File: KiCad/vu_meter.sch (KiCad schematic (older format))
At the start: 74 parts

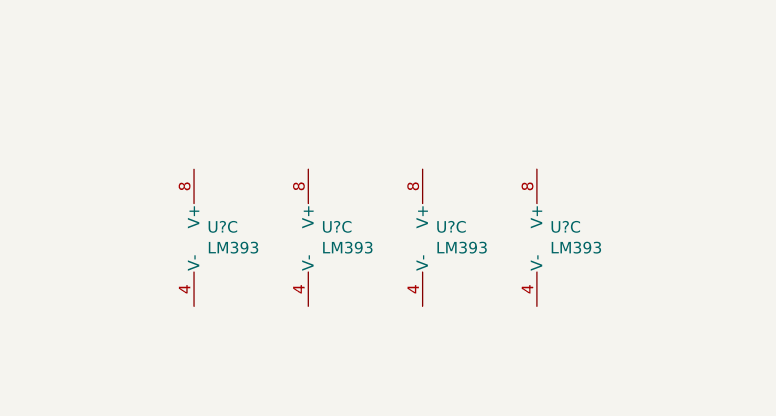
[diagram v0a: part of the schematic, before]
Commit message: freeze at 3 leds
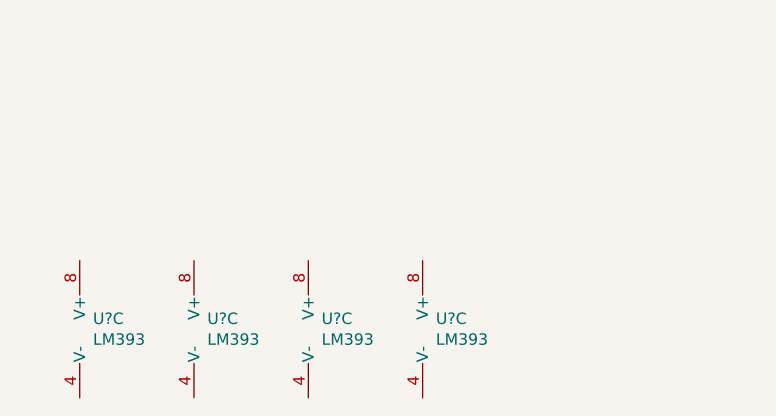
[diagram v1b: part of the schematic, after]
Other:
- moved on the sheet: U?C
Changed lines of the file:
@@
 L Amp-Module-rescue:LM393-Comparator-Amp-Module-rescue U?
 U 3 1 60A35849
-P 1300 6950
+P 800 7350
 AR Path="/604C8E92/60793AB8/60A35849" Ref="U?"  Part="3"
 AR Path="/604C8E92/60A35849" Ref="U?"  Part="3"
 AR Path="/60A35849" Ref="U?"  Part="3"
-F 0 "U?" H 1258 6996 50  0000 L CNN
-F 1 "LM393" H 1258 6905 50  0000 L CNN
-F 2 "" H 1300 6950 50  0001 C CNN
-F 3 "" H 1300 6950 50  0001 C CNN
-	3    1300 6950
+F 0 "U?" H 758 7396 50  0000 L CNN
+F 1 "LM393" H 758 7305 50  0000 L CNN
+F 2 "" H 800 7350 50  0001 C CNN
+F 3 "" H 800 7350 50  0001 C CNN
+	3    800  7350
 	1    0    0    -1
 $EndComp
@@
 L Amp-Module-rescue:LM393-Comparator-Amp-Module-rescue U?
 U 3 1 60A3585D
-P 1800 6950
+P 1300 7350
 AR Path="/604C8E92/60793AB8/60A3585D" Ref="U?"  Part="3"
 AR Path="/604C8E92/60A3585D" Ref="U?"  Part="3"
 AR Path="/60A3585D" Ref="U?"  Part="3"
-F 0 "U?" H 1758 6996 50  0000 L CNN
-F 1 "LM393" H 1758 6905 50  0000 L CNN
-F 2 "" H 1800 6950 50  0001 C CNN
-F 3 "" H 1800 6950 50  0001 C CNN
-	3    1800 6950
+F 0 "U?" H 1258 7396 50  0000 L CNN
+F 1 "LM393" H 1258 7305 50  0000 L CNN
+F 2 "" H 1300 7350 50  0001 C CNN
+F 3 "" H 1300 7350 50  0001 C CNN
+	3    1300 7350
 	1    0    0    -1
 $EndComp
@@
 L Amp-Module-rescue:LM393-Comparator-Amp-Module-rescue U?
 U 3 1 60A35997
-P 2300 6950
+P 1800 7350
 AR Path="/604C8E92/60793AB8/60A35997" Ref="U?"  Part="3"
 AR Path="/604C8E92/60A35997" Ref="U?"  Part="3"
 AR Path="/60A35997" Ref="U?"  Part="3"
-F 0 "U?" H 2258 6996 50  0000 L CNN
-F 1 "LM393" H 2258 6905 50  0000 L CNN
-F 2 "" H 2300 6950 50  0001 C CNN
-F 3 "" H 2300 6950 50  0001 C CNN
-	3    2300 6950
+F 0 "U?" H 1758 7396 50  0000 L CNN
+F 1 "LM393" H 1758 7305 50  0000 L CNN
+F 2 "" H 1800 7350 50  0001 C CNN
+F 3 "" H 1800 7350 50  0001 C CNN
+	3    1800 7350
 	1    0    0    -1
 $EndComp
@@
 L Amp-Module-rescue:LM393-Comparator-Amp-Module-rescue U?
 U 3 1 60A3599D
-P 2800 6950
+P 2300 7350
 AR Path="/604C8E92/60793AB8/60A3599D" Ref="U?"  Part="3"
 AR Path="/604C8E92/60A3599D" Ref="U?"  Part="3"
 AR Path="/60A3599D" Ref="U?"  Part="3"
-F 0 "U?" H 2758 6996 50  0000 L CNN
-F 1 "LM393" H 2758 6905 50  0000 L CNN
-F 2 "" H 2800 6950 50  0001 C CNN
-F 3 "" H 2800 6950 50  0001 C CNN
-	3    2800 6950
-	1    0    0    -1
-$EndComp
+F 0 "U?" H 2258 7396 50  0000 L CNN
+F 1 "LM393" H 2258 7305 50  0000 L CNN
+F 2 "" H 2300 7350 50  0001 C CNN
+F 3 "" H 2300 7350 50  0001 C CNN
+	3    2300 7350
+	1    0    0    -1
+$EndComp

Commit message: schematic completed
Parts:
- removed D? (x3): LED_Small, symbol Device:LED_Small
- removed D?: 3V, symbol Device:D_Zener_Small
- removed D?: 2V, symbol Device:D_Zener_Small
- removed Q? (x4): NPN, symbol Device:Q_NPN_BCE
- removed Q?: PNP, symbol Device:Q_PNP_BCE
- removed R?: 75, symbol Device:R_Small
- removed R?: 20k, symbol Device:R_Small
- removed R?: 15k, symbol Device:R_Small
- removed R?: 23k, symbol Device:R_Small
- removed R? (x6): 10k, symbol Device:R_Small
- removed R?: 100k, symbol Device:R_Small
- removed R?: 150, symbol Device:R_Small
- removed R? (x3): 22k, symbol Device:R_Small
- removed R?: 12k, symbol Device:R_Small
- removed R?: 33k, symbol Device:R_Small
- removed R?: 27k, symbol Device:R_Small
- removed R?: 36k, symbol Device:R_Small
- removed R? (x2): 120k, symbol Device:R_Small
- removed U? (x12): LM393, symbol Amp-Module-rescue:LM393-Comparator-Amp-Module-rescue
- removed U? (x2): OPAMP, symbol pspice:OPAMP
- removed U? (x2): 74LS08, symbol 74xx:74LS08
- added C16, C17: 0.1uF, symbol Device:C_Small
- added D12: 3.5V, symbol Device:D_Zener_Small
- added D15: LED_Small, symbol Device:LED_Small
- added Q10: S9013, symbol Device:Q_NPN_BCE
- added R52: 43k, symbol Device:R_Small
- added R56, R61: 10k, symbol Device:R_Small
- added R65: 22k, symbol Device:R_Small
- added U10, U11: LM393, symbol Comparator:LM393
- D11: renamed from D?; value 3V -> 4.5V
- D13: renamed from D?; value 2V -> 1.5V
- Q11, Q8, Q9: renamed from Q?; value NPN -> S9013
- R49: renamed from R?; value 23k -> 15k
- R50: renamed from R?; value 33k -> 27k
- R51: renamed from R?; value 36k -> 62k
- R53: renamed from R?; value 75 -> 100
- R59: renamed from R?; value 15k -> 10k
- R60: renamed from R?; value 12k -> 10k
- R62: renamed from R?; value 10k -> 2.2k
- R66: renamed from R?; value 22k -> 27k
- R67: renamed from R?; value 20k -> 33k
- R69: renamed from R?; value 27k -> 10k
- gave numbers to parts that had none: 12
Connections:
- net labels added: +5V_REG, V_MON, WARN
- net labels removed: +5VDC, PROTECT1, PROTECT2, TEMPMON12, VOUT1MON, VOUT2MON
- wire segments 172 -> 104
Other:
- note removed: "DUPLICATE"
- moved on the sheet: D11, D13, D14, D16, D17, Q11, Q12, Q7, Q8, Q9, R49, R50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

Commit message: edited chez Gabri's
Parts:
- added R?: 500k, symbol Device:RTRIM
- R49: value 15k -> 12k
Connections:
- net at R50.1, U10.3 (+): now also R?.2; no longer R49.2
- new net: R49.2, R?.1
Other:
- note added: "log(A)"
- moved on the sheet: R28

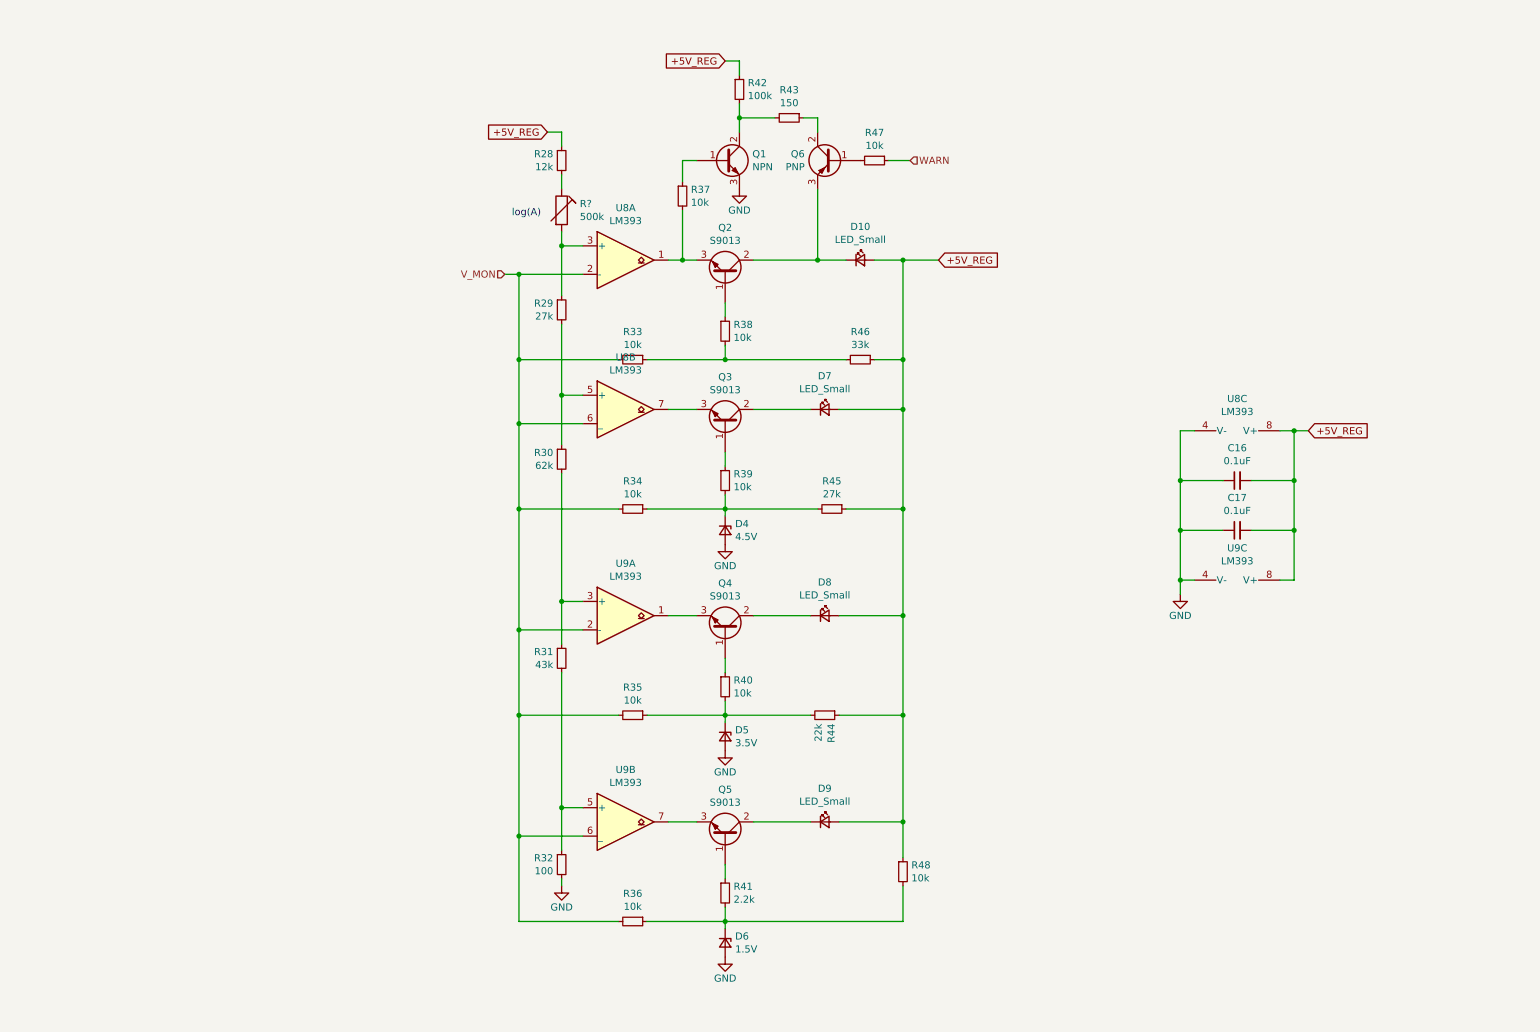
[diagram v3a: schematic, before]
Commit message: added bom
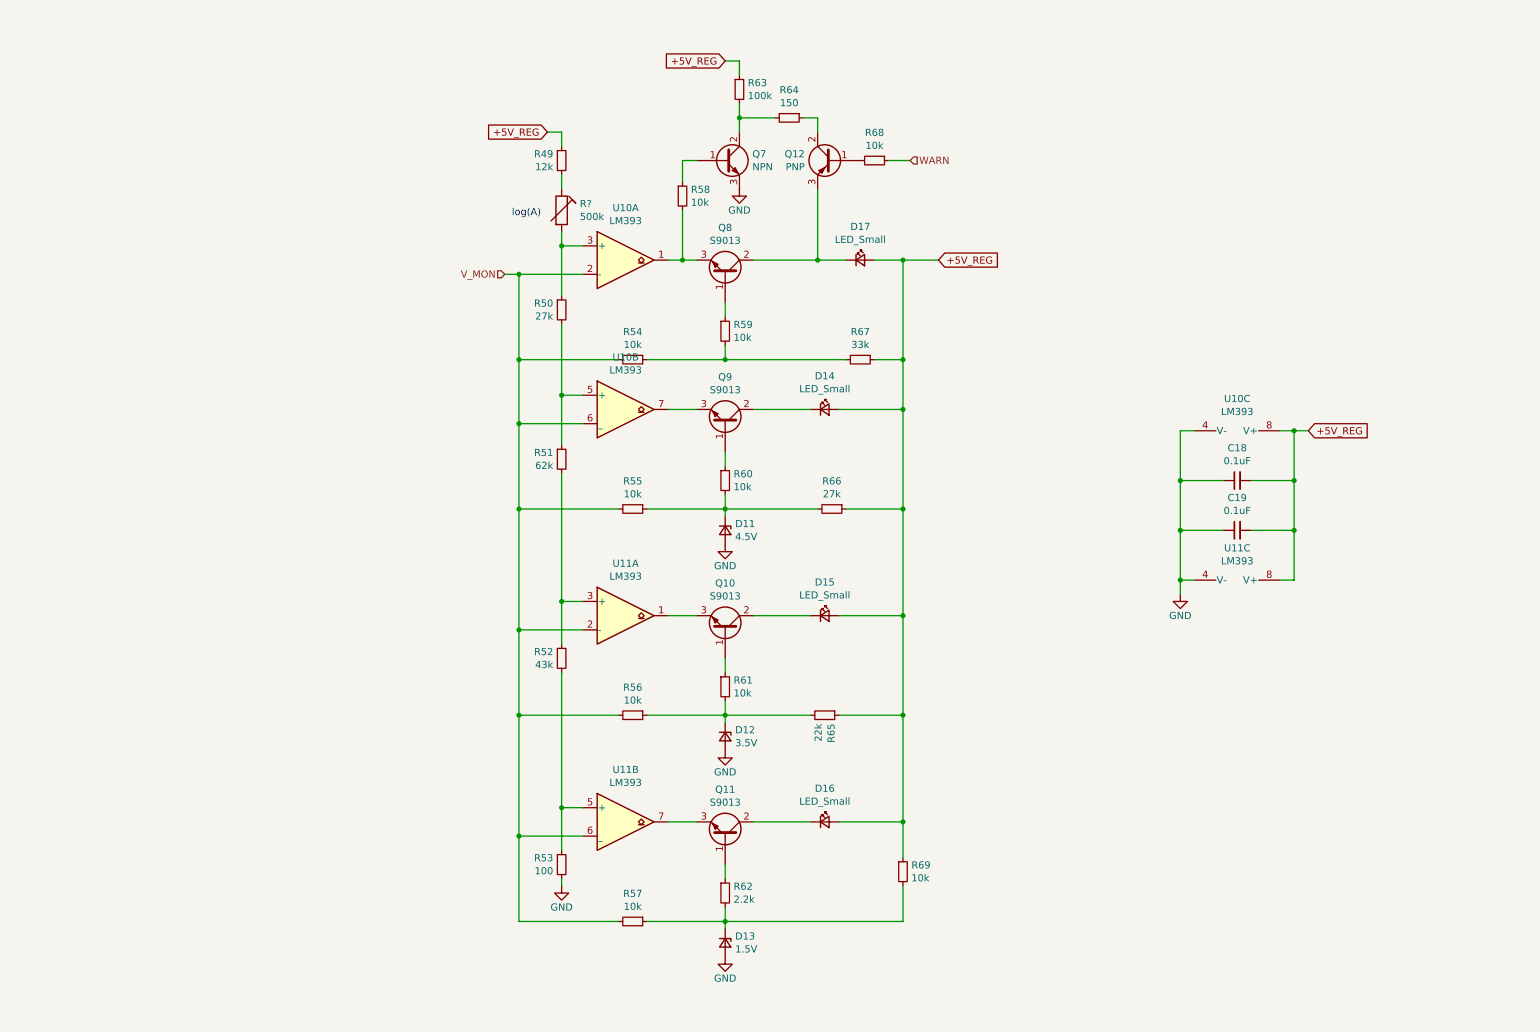
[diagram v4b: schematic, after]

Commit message: finished PCB with TL12
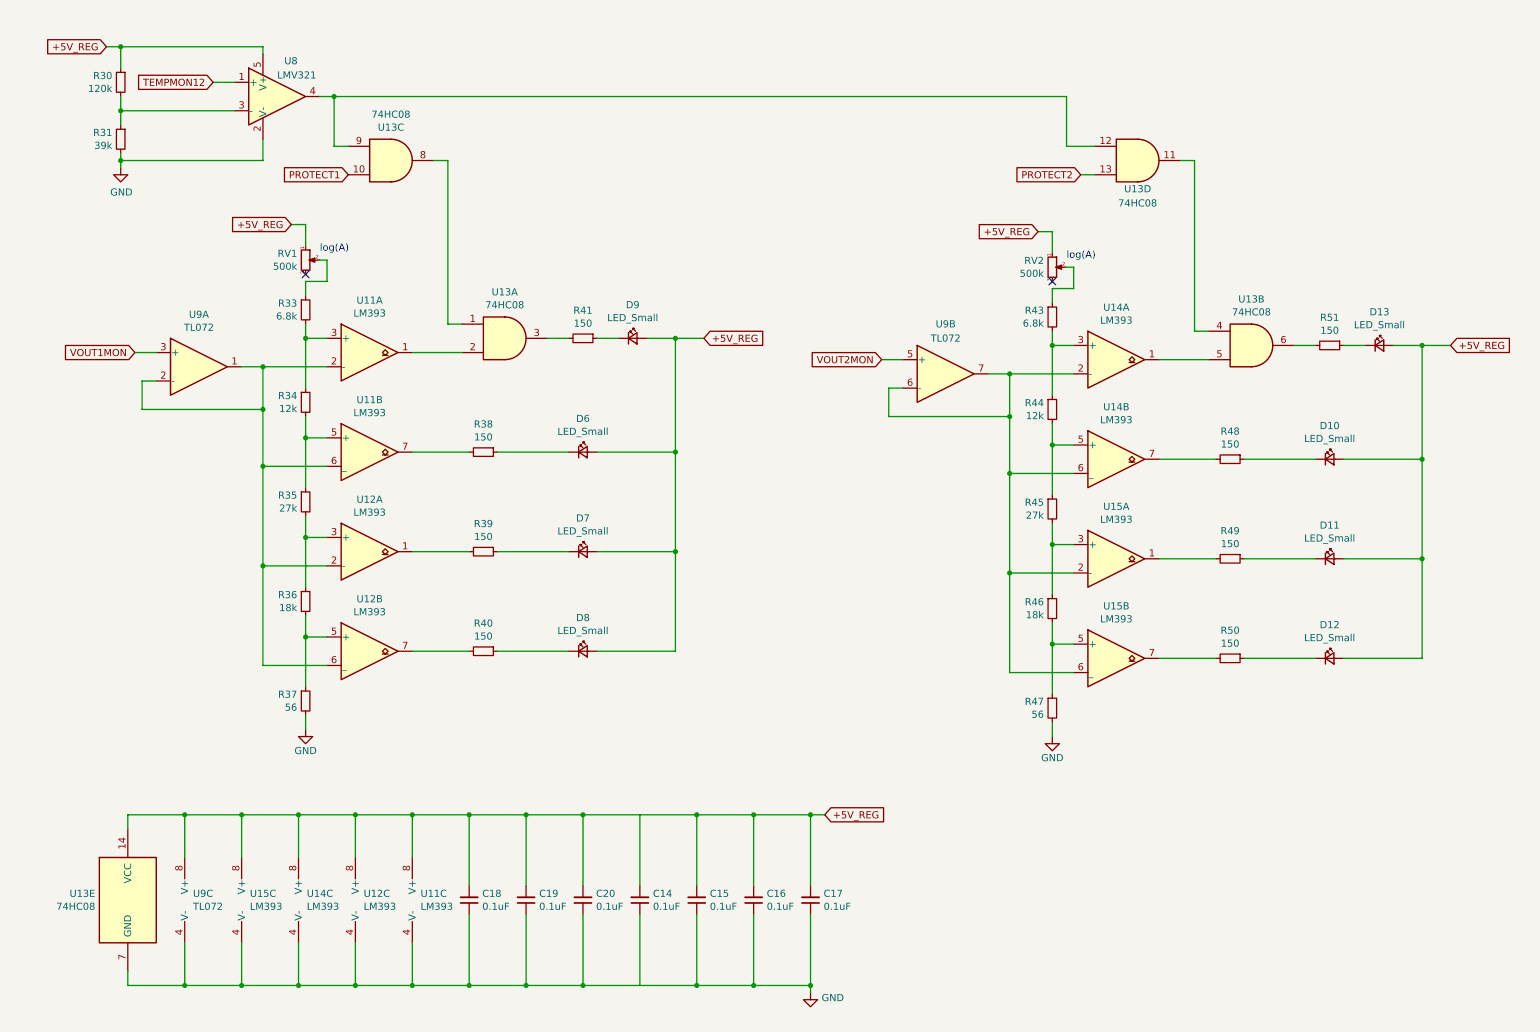
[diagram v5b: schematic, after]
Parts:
- removed D11: 4.5V, symbol Device:D_Zener_Small
- removed D12: 3.5V, symbol Device:D_Zener_Small
- removed D13: 1.5V, symbol Device:D_Zener_Small
- removed Q10, Q11, Q8, Q9: S9013, symbol Device:Q_NPN_BCE
- removed Q12: PNP, symbol Device:Q_PNP_BCE
- removed Q7: NPN, symbol Device:Q_NPN_BCE
- removed R54, R55, R56, R57, R58, R59, R60, R61, R68, R69: 10k, symbol Device:R_Small
- removed R62: 2.2k, symbol Device:R_Small
- removed R63: 100k, symbol Device:R_Small
- removed R64: 150, symbol Device:R_Small
- removed R65: 22k, symbol Device:R_Small
- removed R66: 27k, symbol Device:R_Small
- removed R67: 33k, symbol Device:R_Small
- removed R?: 500k, symbol Device:RTRIM
- added C16, C17, C18, C19, C20: 0.1uF, Capacitor_SMD:C_0805_2012Metric, symbol Device:C_Small
- added D10, D11, D12, D13: LED_Small, LED_THT:LED_Rectangular_W5.0mm_H5.0mm, symbol Device:LED_Small
- added R30: 120k, Resistor_SMD:R_0805_2012Metric, symbol Device:R_Small
- added R31: 39k, Resistor_SMD:R_0805_2012Metric, symbol Device:R_Small
- added R38, R39, R40, R41, R48, R49, R50, R51: 150, Resistor_SMD:R_0805_2012Metric, symbol Device:R_Small
- added R43: 6.8k, Resistor_SMD:R_0805_2012Metric, symbol Device:R_Small
- added R44: 12k, Resistor_SMD:R_0805_2012Metric, symbol Device:R_Small
- added R45: 27k, Resistor_SMD:R_0805_2012Metric, symbol Device:R_Small
- added R46: 18k, Resistor_SMD:R_0805_2012Metric, symbol Device:R_Small
- added R47: 56, Resistor_SMD:R_0805_2012Metric, symbol Device:R_Small
- added RV1, RV2: 500k, AmpModule:Trim_audio, symbol Device:R_POT_Small
- added U13: 74HC08, Package_SO:SOIC-14_3.9x8.7mm_P1.27mm, symbol 74xx:74LS08
- added U14, U15: LM393, Package_SO:SOIC-8_3.9x4.9mm_P1.27mm, symbol Comparator:LM393
- added U8: LMV321, Package_TO_SOT_SMD:SOT-23-5, symbol Amplifier_Operational:LMV321
- added U9: TL072, Package_SO:SOIC-8_3.9x4.9mm_P1.27mm, symbol Amplifier_Operational:TL072
- C14: renamed from C16; footprint (none) -> Capacitor_SMD:C_0805_2012Metric
- C15: renamed from C17; footprint (none) -> Capacitor_SMD:C_0805_2012Metric
- D6: renamed from D14; footprint (none) -> LED_THT:LED_Rectangular_W5.0mm_H5.0mm
- D7: renamed from D15; footprint (none) -> LED_THT:LED_Rectangular_W5.0mm_H5.0mm
- D8: renamed from D16; footprint (none) -> LED_THT:LED_Rectangular_W5.0mm_H5.0mm
- D9: renamed from D17; footprint (none) -> LED_THT:LED_Rectangular_W5.0mm_H5.0mm
- R33: renamed from R49; value 12k -> 6.8k; footprint (none) -> Resistor_SMD:R_0805_2012Metric
- R34: renamed from R50; value 27k -> 12k; footprint (none) -> Resistor_SMD:R_0805_2012Metric
- R35: renamed from R51; value 62k -> 27k; footprint (none) -> Resistor_SMD:R_0805_2012Metric
- R36: renamed from R52; value 43k -> 18k; footprint (none) -> Resistor_SMD:R_0805_2012Metric
- R37: renamed from R53; value 100 -> 56; footprint (none) -> Resistor_SMD:R_0805_2012Metric
- U11: renamed from U10; footprint (none) -> Package_SO:SOIC-8_3.9x4.9mm_P1.27mm
- U12: renamed from U11; footprint (none) -> Package_SO:SOIC-8_3.9x4.9mm_P1.27mm
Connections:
- net +5V_REG: now also C16.2, C17.2, C18.2, C19.2, C20.2, D10.2 (A), D11.2 (A), D12.2 (A), D13.2 (A), R30.1, RV1.1, RV2.1, U13.14 (VCC), U14.8 (V+), U15.8 (V+), U8.5 (V+), U9.8 (V+); no longer R33.1
- net GND: now also C16.1, C17.1, C18.1, C19.1, C20.1, R31.2, R47.2, U13.7 (GND), U14.4 (V-), U15.4 (V-), U8.2 (V-), U9.4 (V-)
- net at D9.1 (K): now also R41.1
- net at U11.1: now also U13.2
- net at R33.2: now also R34.1, U11.3 (+)
- net at D6.1 (K): now also R38.1
- net at U11.7: now also R38.2
- net at D8.1 (K): now also R40.1
- net at U12.7: now also R40.2
- net at D7.1 (K): now also R39.1
- net at U12.1: now also R39.2
- net V_MON: no longer names the net of U11.2 (-), U11.6 (_), U12.2 (-), U12.6 (_)
- net V_MON: now also U9.1, U9.2 (-)
- new net: R33.1, RV1.2
- new net: R30.2, R31.1, U8.3 (-)
- new net: U13.11, U13.4
- new net: U13.12, U13.9, U8.4
- new net: U13.1, U13.8
- new net: U14.2 (-), U14.6 (_), U15.2 (-), U15.6 (_), U9.6 (-), U9.7
- new net: R41.2, U13.3
- new net: U13.5, U14.1
- new net: R51.2, U13.6
- new net: R46.2, R47.1, U15.5 (+)
- new net: D13.1 (K), R51.1
- new net: R43.1, RV2.2
- new net: R43.2, R44.1, U14.3 (+)
- new net: D10.1 (K), R48.1
- new net: R44.2, R45.1, U14.5 (+)
- new net: D12.1 (K), R50.1
- new net: R45.2, R46.1, U15.3 (+)
- new net: D11.1 (K), R49.1
- new net: R50.2, U15.7
- new net: R49.2, U15.1
- new net: R48.2, U14.7
- new net PROTECT1: U13.10
- new net PROTECT2: U13.13
- new net TEMPMON12: U8.1 (+)
- new net VOUT1MON: U9.3 (+)
- new net VOUT2MON: U9.5 (+)
- no-connect marks 0 -> 2
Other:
- moved on the sheet: C14, C15, D6, D7, D8, D9, R33, R34, R35, R36, R37, U11A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

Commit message: started BOM export
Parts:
- renumbered C18 to C15, C19 to C16, C20 to C17, C14 to C18, C15 to C19, C16 to C20, C17 to C21, R33 to R32, R34 to R33, R35 to R34, R36 to R35, R37 to R36, R38 to R37, R39 to R38, R40 to R39, R41 to R40, R43 to R41, R44 to R42, R45 to R43, R46 to R44, R47 to R45, R48 to R46, R49 to R47, R50 to R48, R51 to R49, U15 to U10, U11 to U10, U8 to U11, U14 to U12, U14 to U13, U12 to U13, U15 to U14, U11 to U14, U13 to U8
